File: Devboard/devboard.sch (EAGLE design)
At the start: 116 parts, among them J1 USB-MICROB-2, J10 MJ-2509N, J11 MJ-2509N, J12 MJ-2509N, J13 MJ-2509N, J6 USB-A-HU, J7 USB-A-HU, J8 USB-A-HU, J9 USB-A-HU, Q1 2.5A/30V/105mΩ, T1 BSS138PS, U1 PCA9634PW, U4 3.3V

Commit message: Revised dev board PCB layout Added rough draft BOM
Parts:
- removed C13: 0.1uF/16V, vibhud:CAPACITOR-0805
- removed C14: 10uF/25V, vibhud:CAPACITOR_POLPANASONIC_D
- removed C15, C16: 2.2uF/16V, vibhud:CAPACITOR-1206
- removed J18: (no value), vibhud:CONN_02LOCK
- removed R11, R16, R17, R21, R25: 10k, vibhud:RESISTOR0805
- removed R12, R22, R23, R24, R26, R27, R28, R29, R30, R31, R40, R41, R42, R43, R44, R45, R46: 330R, vibhud:RESISTOR0805
- removed R18, R19, R20: 0.43R, vibhud:RESISTOR0805
- removed R32, R33, R34, R35, R36, R37, R38, R39: 510R, vibhud:RESISTOR0805
- removed R47, R48, R49: 1k, vibhud:RESISTOR0805
- added C1, C2, C4: 1.0uF, vibhud:CAPACITOR-0805
- added C3: 100uF/6.3V, vibhud:CAPACITOR-1206
- added J14: 1x8M, vibhud:CONN_08LOCK
- added RN1, RN2, RN3, RN4, RN5, RN6, RN7: 1k, vibhud:4R-NEXBS8V
- added RN8, RN9: 10k, vibhud:4R-NEXBS8V
- C10: value 10uF/16V -> 0.1uF/16V; device vibhud:CAPACITOR-1206 -> vibhud:CAPACITOR-0805
- C11: value 0.1uF/16V -> 2.2uF/16V; device vibhud:CAPACITOR-0805 -> vibhud:CAPACITOR-1206
- C12: value 10uF/16V -> 10uF/25V; device vibhud:CAPACITOR-1206 -> vibhud:CAPACITOR_POLPANASONIC_D
- C5: value 1.0uF -> 10uF
- C6: value 1.0uF -> 10uF/16V; device vibhud:CAPACITOR-0805 -> vibhud:CAPACITOR-1206
- C7: value 100uF/6.3V -> 0.1uF/16V; device vibhud:CAPACITOR-1206 -> vibhud:CAPACITOR-0805
- C8: value 1.0uF -> 2.2uF/16V; device vibhud:CAPACITOR-0805 -> vibhud:CAPACITOR-1206
- C9: value 10uF -> 10uF/16V; device vibhud:CAPACITOR-0805 -> vibhud:CAPACITOR-1206
- D10, D11, D12, D21, D22, D23, D24, D25, D26, D27, D28, D4, D5, D6, D7, D8, D9: value (none) -> Blue
- D13, D14, D15, D16, D17, D18, D19, D20: value (none) -> Red
- FLASH, RESET: value MOMENTARY-SWITCH-SPST-SMD-6.0X3.5MM -> MOMENTARY-SWITCH-SPST-PTH-6.0MM; device vibhud:MOMENTARY-SWITCH-SPST-SMD-6.0X3.5MM -> vibhud:MOMENTARY-SWITCH-SPST-PTH-6.0MM
- J15, J16: value (none) -> 1x8F; device vibhud:CONN_08LOCK -> vibhud:CONN_08FEMALE_LOCK
- J17: value (none) -> 1x2M; device vibhud:CONN_08LOCK -> vibhud:CONN_02LOCK_LONGPADS
- J2: value (none) -> 1x2M
- J3, J4: value (none) -> 1x8F
- J5: value (none) -> 1x8M
- R1: value 10k -> 51R
- R4: value 51R -> 10k
- R5: value 0.43R -> 10k
- R6, R7, R8, R9: value 10k -> 0.43R
- U2, U3: value (none) -> DRV8833C
- X1: value (none) -> ESP12
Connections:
- removed net N$12: D10.A, R29.2
- removed net N$13: D11.A, R30.2
- removed net N$14: D12.A, R31.2
- new net N$2: D5.C, RN1A.2
- new net N$3: D6.C, RN1B.2
- new net N$8: D9.C, RN2A.2
- net 3.3V: now also C2.1, C3.1, C4.1, C5.1, RN7D.2, RN8A.1, RN8B.1, RN8C.1, RN8D.1, RN9A.2, RN9B.2, RN9C.2; no longer C6.1, C7.1, C8.1, C9.1, R1.2, R11.2, R12.2, R17.1, R25.2, R6.1, R7.2, R8.2
- net 5V: now also C1.1, C10.1, C12.+, C6.2, C7.1, C9.2, R4.1; no longer C10.2, C11.1, C12.2, C13.1, C14.+, C5.1, R9.1
- net A_ISENSE0: now also R6.2; no longer R18.2
- net A_ISENSE1: now also R8.2; no longer R20.2
- net B_ISENSE0: now also R7.2; no longer R5.2
- net B_ISENSE1: now also R9.2; no longer R19.2
- net CH_PD: now also RN8B.2; no longer R11.1
- net CP3V3: now also J16.2; no longer J17.2
- net CTS: now also J15.8; no longer J16.8
- net DCD: now also J15.2; no longer J16.2
- net DSR: now also J15.4; no longer J16.4
- net DTR: now also RN7C.2; no longer R49.2
- net GND: now also C1.2, C11.1, C12.-, C2.2, C3.2, C4.2, C6.1, C8.1, C9.1, FLASH.2, J16.3, R6.1, R7.1, R8.1, R9.1, RN1A.1, RN1B.1, RN1C.1, RN1D.1, RN2A.1, RN2B.1, RN2C.1, RN2D.1, RN9D.2; no longer C10.1, C12.1, C14.-, C15.1, C16.1, C6.2, C7.2, C8.2, C9.2, D10.C, D11.C, D12.C, D5.C, D6.C, D7.C, D8.C, D9.C, FLASH.1, J17.3, R16.2, R18.1, R19.1, R20.1, R21.1
- net GPIO0: now also FLASH.1, RN8D.2; no longer FLASH.2, R25.1
- net GPIO12: now also R1.2; no longer R4.2
- net GPIO14: now also RN8C.2; no longer R1.1
- net GPIO15: now also RN9D.1; no longer R16.1
- net GPIO2: now also RN9C.1; no longer R7.1
- net IO2: now also J16.6; no longer J17.6
- net IO3: now also J16.5; no longer J17.5
- net LED_G: now also R1.1; no longer R4.1
- net MOT_0N: now also J14.2, RN3C.1, RN3D.1; no longer J15.2, R33.1, R40.1
- net MOT_0P: now also J14.1, RN3A.1, RN3B.1; no longer J15.1, R23.1, R32.1
- net MOT_1N: now also J14.4, RN4C.1, RN4D.1; no longer J15.4, R35.1, R42.1
- net MOT_1P: now also J14.3, RN4A.1, RN4B.1; no longer J15.3, R34.1, R41.1
- net MOT_2N: now also J14.6, RN5C.1, RN5D.1; no longer J15.6, R37.1, R44.1
- net MOT_2P: now also J14.5, RN5A.1, RN5B.1; no longer J15.5, R36.1, R43.1
- net MOT_3N: now also J14.8, RN6C.1, RN6D.1; no longer J15.8, R39.1, R46.1
- net MOT_3P: now also J14.7, RN6A.1, RN6B.1; no longer J15.7, R38.1, R45.1
- net N$1: now also R4.2; no longer R9.2
- net N$10: now also D11.C, RN2C.2; no longer D8.A, R27.2
- net N$11: now also D12.C, RN2D.2; no longer D9.A, R28.2
- net N$15: now also RN3B.2; no longer R23.2
- net N$16: now also RN3A.2; no longer R32.2
- net N$17: now also RN3C.2; no longer R33.2
- net N$18: now also RN4A.2; no longer R34.2
- net N$19: now also RN4C.2; no longer R35.2
- net N$20: now also RN5A.2; no longer R36.2
- net N$21: now also RN5C.2; no longer R37.2
- net N$22: now also RN6A.2; no longer R38.2
- net N$23: now also RN6C.2; no longer R39.2
- net N$24: now also RN3D.2; no longer R40.2
- net N$25: now also RN4B.2; no longer R41.2
- net N$26: now also RN4D.2; no longer R42.2
- net N$27: now also RN6D.2; no longer R46.2
- net N$28: now also RN6B.2; no longer R45.2
- net N$29: now also RN5D.2; no longer R44.2
- net N$30: now also RN5B.2; no longer R43.2
- net N$31: now also J16.1, J17.2; no longer J17.1, J18.2
- net N$6: now also D7.C, RN1C.2; no longer D5.A, R22.2
- net N$7: now also D8.C, RN1D.2; no longer D6.A, R24.2
- net N$9: now also D10.C, RN2B.2; no longer D7.A, R26.2
- net PWM0: now also D5.A, U2.A_IN1; no longer R22.1, U2.B_IN1
- net PWM1: now also D6.A, U2.A_IN2; no longer R24.1, U2.B_IN2
- net PWM2: now also D7.A, U2.B_IN1; no longer R26.1, U2.A_IN2
- net PWM3: now also D8.A, U2.B_IN2; no longer R27.1, U2.A_IN1
- net PWM4: now also D9.A, U3.A_IN1; no longer R28.1, U3.A_IN2
- net PWM5: now also D10.A, U3.A_IN2; no longer R29.1, U3.A_IN1
- net PWM6: now also D11.A, U3.B_IN1; no longer R30.1, U3.B_IN2
- net PWM7: now also D12.A, U3.B_IN2; no longer R31.1, U3.B_IN1
- net PWR_LED: now also RN7D.1; no longer R12.1
- net RESET: now also RN8A.2; no longer R8.1
- net RI: now also J15.1; no longer J16.1
- net RST: now also J16.4; no longer J17.4
- net RTS: now also RN7A.2; no longer R48.2
- net RXD0: now also RN7B.2; no longer R47.2
- net SCL: now also RN9B.1; no longer R17.2
- net SDA: now also RN9A.1; no longer R6.2
- net SU: now also J16.8; no longer J17.8
- net SU#: now also J16.7; no longer J17.7
- net TXD0: now also J15.6; no longer J16.6
- net USB_DTR: now also J15.3, RN7C.1; no longer J16.3, R49.1
- net USB_RTS: now also J15.7, RN7A.1; no longer J16.7, R48.1
- net USB_RXD: now also J15.5, RN7B.1; no longer J16.5, R47.1
- net VCP0: now also C7.2; no longer C11.2
- net VCP1: now also C10.2; no longer C13.2
- net VINT0: now also C8.2; no longer C16.2
- net VINT1: now also C11.2; no longer C15.2
- net V_USB: now also J17.1, R5.2; no longer J18.1, R21.2
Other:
- moved on the sheet: C10, C11, C5, D10, D11, D12, D13, D14, D15, D16, D17, D18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

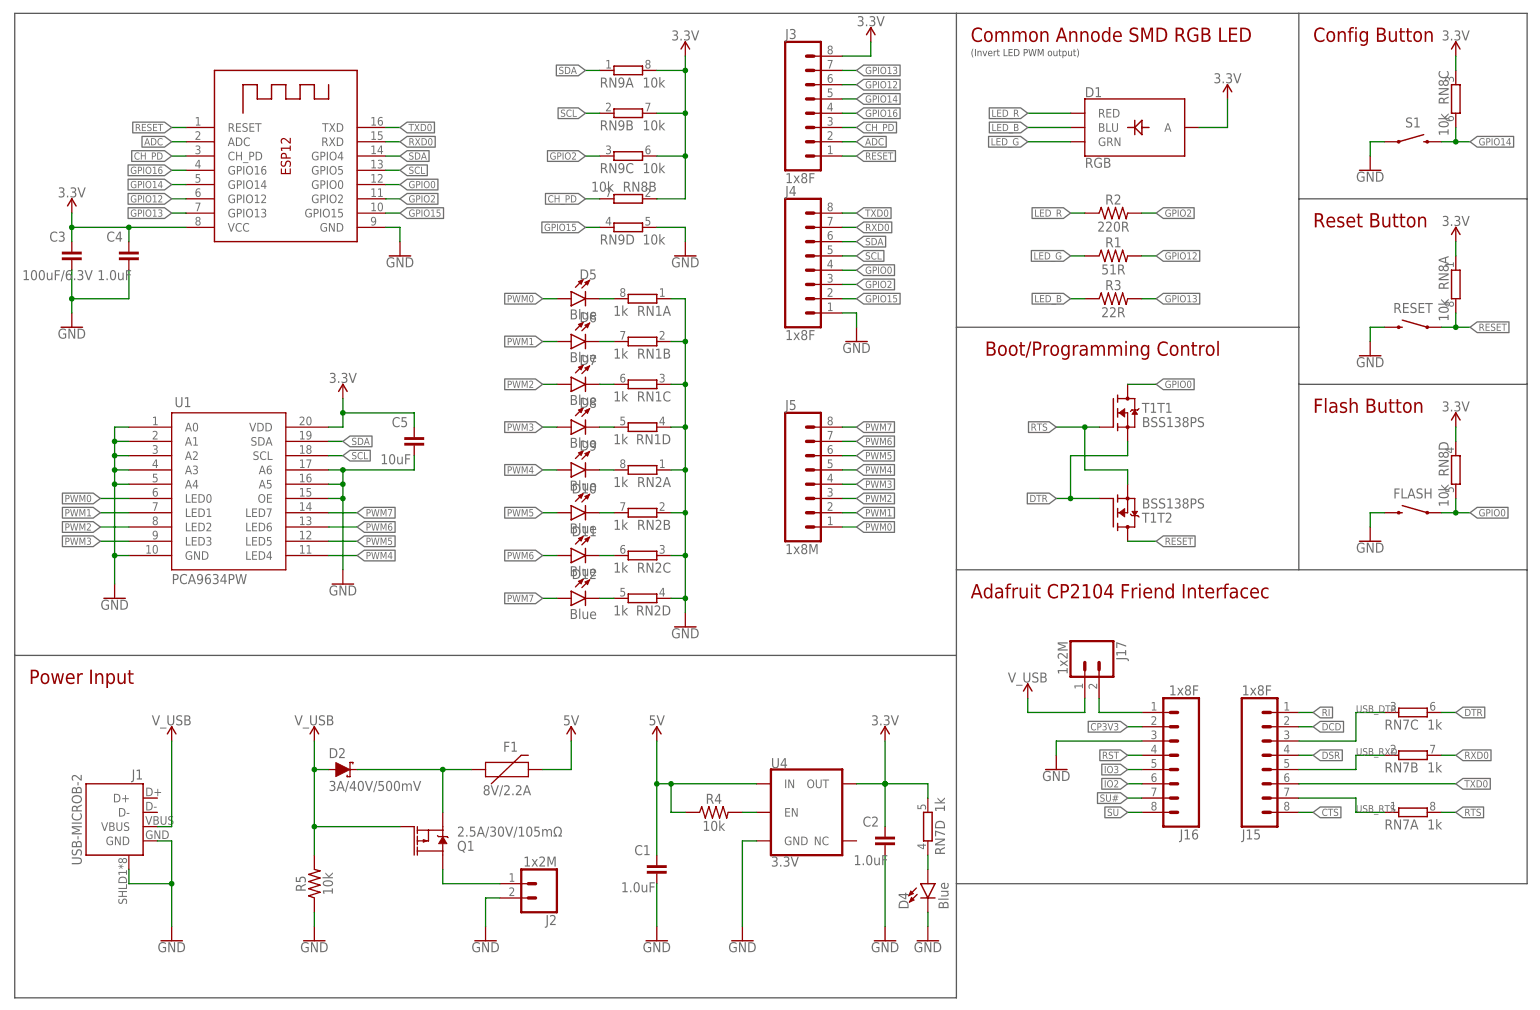
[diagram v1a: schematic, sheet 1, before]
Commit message: Updated dev board, replaced some parts that are not generally available
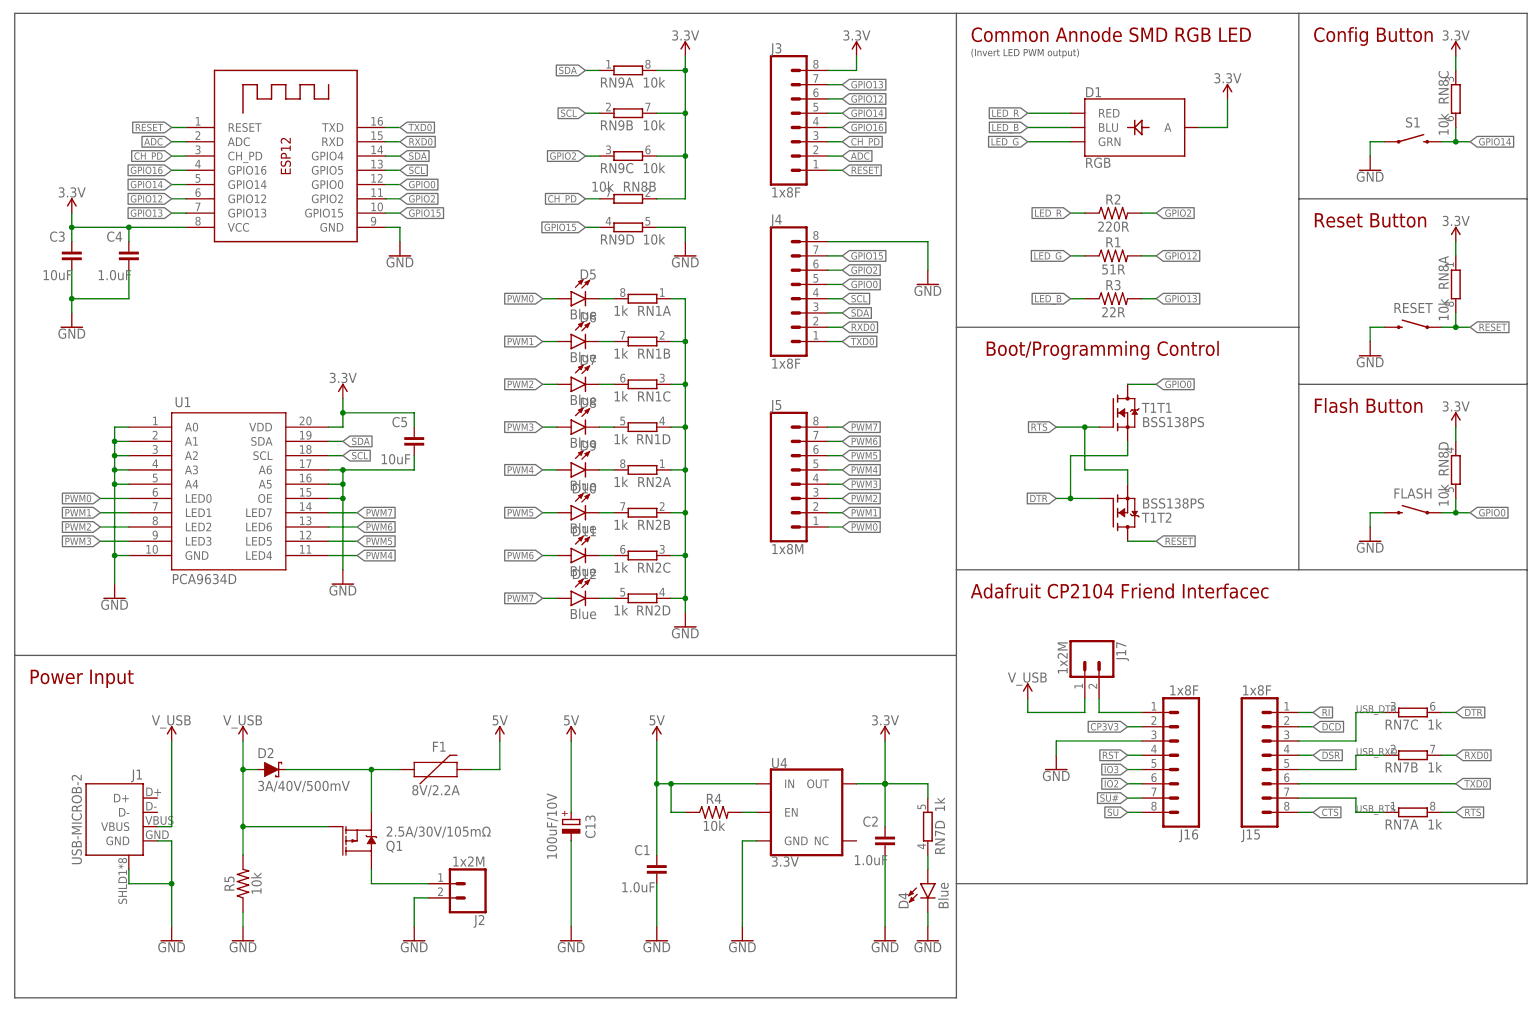
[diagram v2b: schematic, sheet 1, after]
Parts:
- removed C12: 10uF/25V, vibhud:CAPACITOR_POLPANASONIC_D
- added C13: 100uF/10V, vibhud:CAPACITOR_POLPANASONIC_D
- C1, C2, C4, C5: device vibhud:CAPACITOR-0805 -> vibhud:CAPACITOR-1206
- C10, C7: value 0.1uF/16V -> 0.1uF; device vibhud:CAPACITOR-0805 -> vibhud:CAPACITOR-1206
- C11, C8: value 2.2uF/16V -> 2.2uF
- C3: value 100uF/6.3V -> 10uF
- C6, C9: value 10uF/16V -> 10uF
- U1: value PCA9634PW -> PCA9634D; device vibhud:PCA9634 -> vibhud:PCA963420-SO
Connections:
- net 5V: now also C13.+; no longer C12.+
- net GND: now also C13.-, J4.8; no longer C12.-, J4.1
- net GPIO0: now also J4.5; no longer J4.4
- net GPIO15: now also J4.7; no longer J4.2
- net GPIO2: now also J4.6; no longer J4.3
- net RXD0: now also J4.2; no longer J4.7
- net SCL: now also J4.4; no longer J4.5
- net SDA: now also J4.3; no longer J4.6
- net TXD0: now also J4.1; no longer J4.8
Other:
- moved on the sheet: D2, F1, J2, J3, J4, J5, Q1, R5

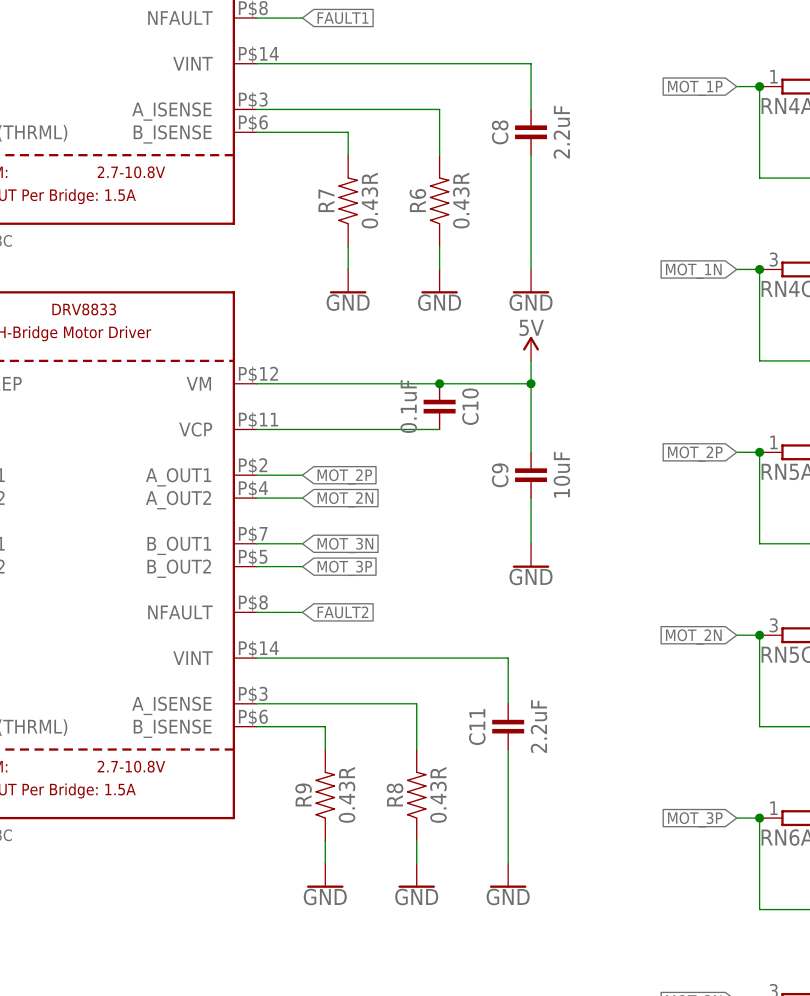
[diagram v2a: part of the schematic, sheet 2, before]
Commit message: Increased motor driver current
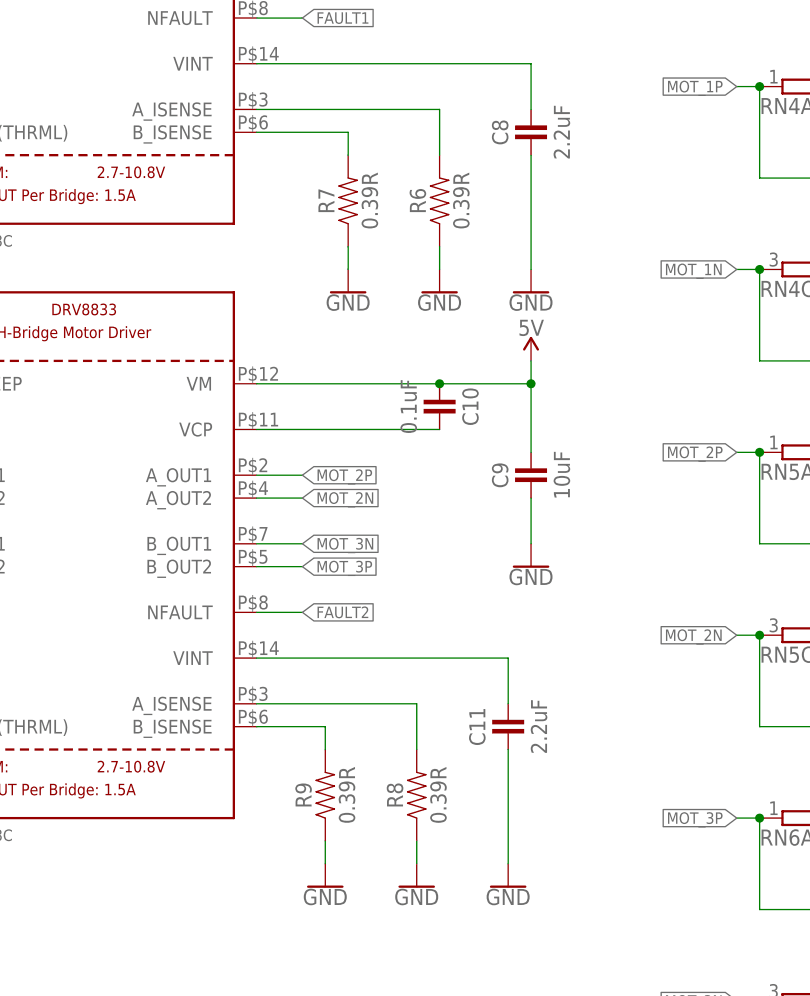
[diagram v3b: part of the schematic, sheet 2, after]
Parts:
- R6, R7, R8, R9: value 0.43R -> 0.39R
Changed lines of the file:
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@@
 <part name="U3" library="vibhud" library_urn="urn:adsk.eagle:library:2530795" deviceset="DRV8833" device="" package3d_urn="urn:adsk.eagle:package:2531169/1" value="DRV8833C"/>
 <part name="C8" library="vibhud" library_urn="urn:adsk.eagle:library:2530795" deviceset="CAPACITOR" device="-1206" package3d_urn="urn:adsk.eagle:package:2531037/1" value="2.2uF"/>
-<part name="R7" library="vibhud" library_urn="urn:adsk.eagle:library:2530795" deviceset="RESISTOR" device="0805" package3d_urn="urn:adsk.eagle:package:2531030/1" value="0.43R"/>
-<part name="R6" library="vibhud" library_urn="urn:adsk.eagle:library:2530795" deviceset="RESISTOR" device="0805" package3d_urn="urn:adsk.eagle:package:2531030/1" value="0.43R"/>
-<part name="R9" library="vibhud" library_urn="urn:adsk.eagle:library:2530795" deviceset="RESISTOR" device="0805" package3d_urn="urn:adsk.eagle:package:2531030/1" value="0.43R"/>
-<part name="R8" library="vibhud" library_urn="urn:adsk.eagle:library:2530795" deviceset="RESISTOR" device="0805" package3d_urn="urn:adsk.eagle:package:2531030/1" value="0.43R"/>
+<part name="R7" library="vibhud" library_urn="urn:adsk.eagle:library:2530795" deviceset="RESISTOR" device="0805" package3d_urn="urn:adsk.eagle:package:2531030/1" value="0.39R"/>
+<part name="R6" library="vibhud" library_urn="urn:adsk.eagle:library:2530795" deviceset="RESISTOR" device="0805" package3d_urn="urn:adsk.eagle:package:2531030/1" value="0.39R"/>
+<part name="R9" library="vibhud" library_urn="urn:adsk.eagle:library:2530795" deviceset="RESISTOR" device="0805" package3d_urn="urn:adsk.eagle:package:2531030/1" value="0.39R"/>
+<part name="R8" library="vibhud" library_urn="urn:adsk.eagle:library:2530795" deviceset="RESISTOR" device="0805" package3d_urn="urn:adsk.eagle:package:2531030/1" value="0.39R"/>
 <part name="GND7" library="vibhud" library_urn="urn:adsk.eagle:library:2530795" deviceset="GND" device=""/>
 <part name="GND11" library="vibhud" library_urn="urn:adsk.eagle:library:2530795" deviceset="GND" device=""/>

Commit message: Final changes to dev board for manufacture
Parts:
- FLASH, RESET: value MOMENTARY-SWITCH-SPST-PTH-6.0MM -> MOMENTARY-SWITCH-SPST-SMD-6.0X3.5MM; device vibhud:MOMENTARY-SWITCH-SPST-PTH-6.0MM -> vibhud:MOMENTARY-SWITCH-SPST-SMD-6.0X3.5MM
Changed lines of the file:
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@@
 <part name="GND2" library="vibhud" library_urn="urn:adsk.eagle:library:2530795" deviceset="GND" device=""/>
 <part name="GND4" library="vibhud" library_urn="urn:adsk.eagle:library:2530795" deviceset="GND" device=""/>
-<part name="RESET" library="vibhud" library_urn="urn:adsk.eagle:library:2530795" deviceset="MOMENTARY-SWITCH-SPST" device="-PTH-6.0MM" package3d_urn="urn:adsk.eagle:package:2531013/1" value="MOMENTARY-SWITCH-SPST-PTH-6.0MM"/>
+<part name="RESET" library="vibhud" library_urn="urn:adsk.eagle:library:2530795" deviceset="MOMENTARY-SWITCH-SPST" device="-SMD-6.0X3.5MM" package3d_urn="urn:adsk.eagle:package:2531010/1" value="MOMENTARY-SWITCH-SPST-SMD-6.0X3.5MM"/>
 <part name="SUPPLY5" library="vibhud" library_urn="urn:adsk.eagle:library:2530795" deviceset="3.3V" device=""/>
 <part name="GND8" library="vibhud" library_urn="urn:adsk.eagle:library:2530795" deviceset="GND" device=""/>
@@
 <part name="U1" library="vibhud" library_urn="urn:adsk.eagle:library:2530795" deviceset="PCA9634" device="20-SO" package3d_urn="urn:adsk.eagle:package:3162409/1" value="PCA9634D"/>
 <part name="GND16" library="vibhud" library_urn="urn:adsk.eagle:library:2530795" deviceset="GND" device=""/>
-<part name="FLASH" library="vibhud" library_urn="urn:adsk.eagle:library:2530795" deviceset="MOMENTARY-SWITCH-SPST" device="-PTH-6.0MM" package3d_urn="urn:adsk.eagle:package:2531013/1" value="MOMENTARY-SWITCH-SPST-PTH-6.0MM"/>
+<part name="FLASH" library="vibhud" library_urn="urn:adsk.eagle:library:2530795" deviceset="MOMENTARY-SWITCH-SPST" device="-SMD-6.0X3.5MM" package3d_urn="urn:adsk.eagle:package:2531010/1" value="MOMENTARY-SWITCH-SPST-SMD-6.0X3.5MM"/>
 <part name="SUPPLY3" library="vibhud" library_urn="urn:adsk.eagle:library:2530795" deviceset="3.3V" device=""/>
 <part name="GND17" library="vibhud" library_urn="urn:adsk.eagle:library:2530795" deviceset="GND" device=""/>
